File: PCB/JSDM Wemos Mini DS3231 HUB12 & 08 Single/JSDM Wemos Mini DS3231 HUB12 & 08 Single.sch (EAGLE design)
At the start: 14 parts, among them X1 PSU

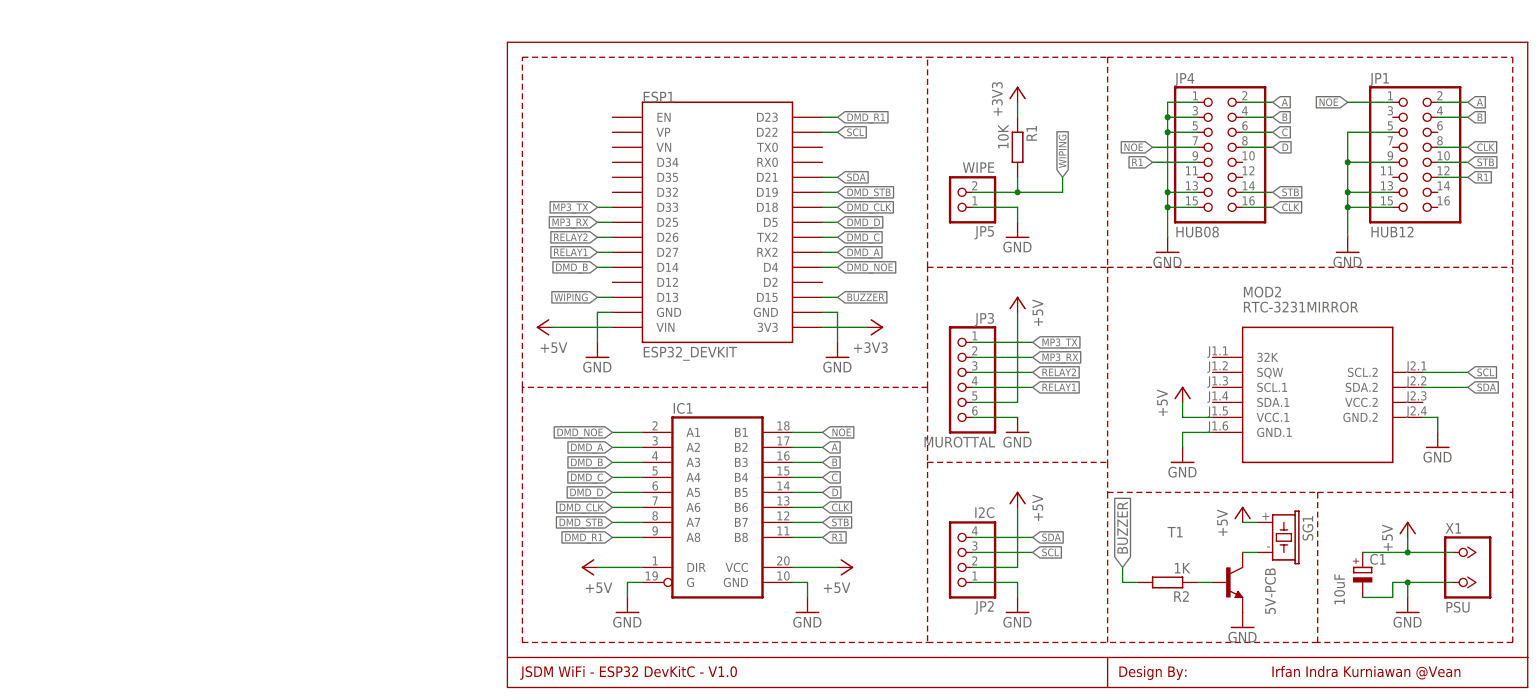
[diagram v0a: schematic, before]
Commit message: JSDM PCB Single Layer ESP8266 + ESP32
Desain PCB SIngle Layer versi:
- Wemos D1 mini HUB12 + HUB08
- Wemos D1 Mini 3x HUB12
- ESP32 Devkit HUB12 + HUB08
- ESP32 Devkit Mini 3x HUB12
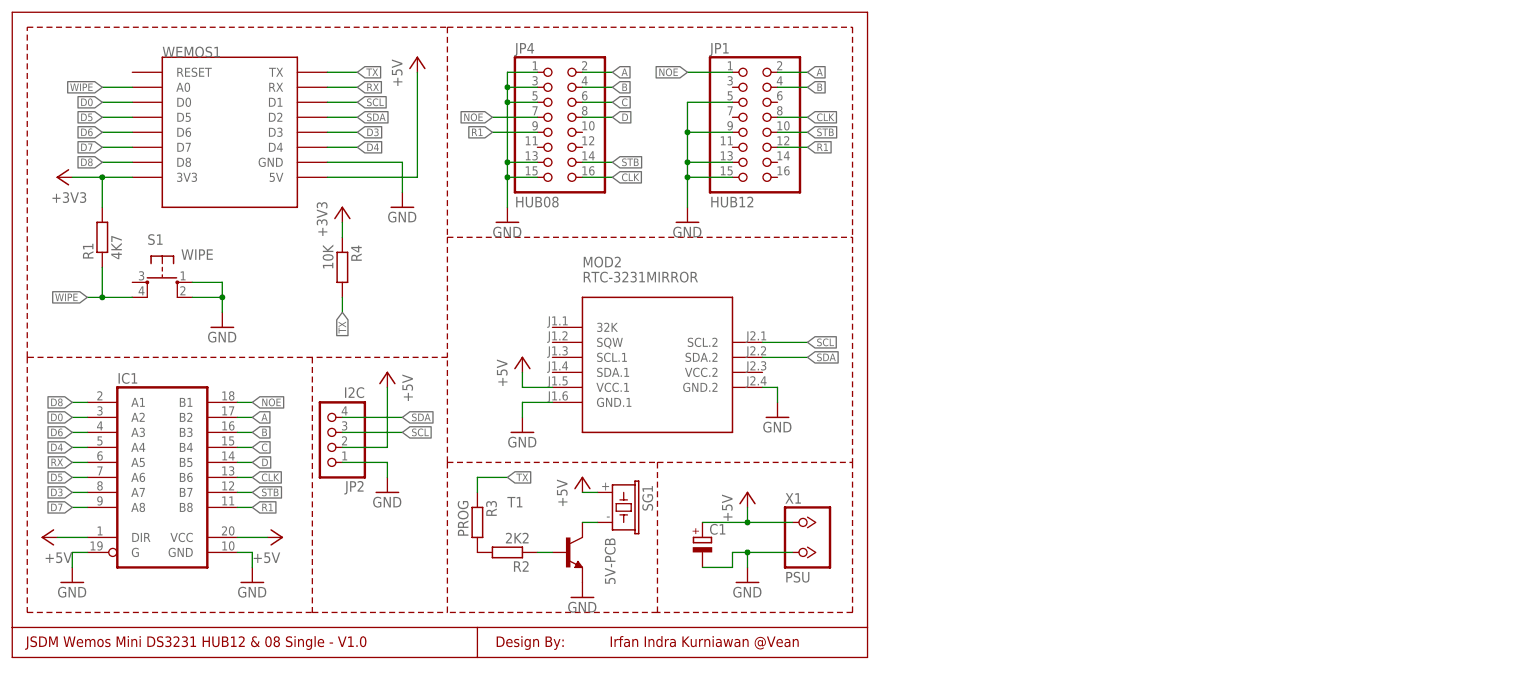
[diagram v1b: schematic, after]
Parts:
- removed ESP1: ESP32_DEVKIT, DOIT_ESP32_DEVKIT:ESP32_DEVKIT
- removed JP3: MUROTTAL, FansElectronics-Header:PINHD-1X6
- removed JP5: WIPE, FansElectronics-Header:PINHD-1X2
- added R3: PROG, FansElectronics-RCL:R-EU_M0805
- added R4: 10K, FansElectronics-RCL:R-EU_0207/12
- added S1: WIPE, FansElectronics-Switch:TACT-6X6OCT
- added WEMOS1: (no value), esp8266modules:WEMOS-D1-MINI
- C1: value 10uF -> (none)
- R1: value 10K -> 4K7; device FansElectronics-RCL:R-EU_0207/7 -> FansElectronics-RCL:R-EU_0207/12
- R2: value 1K -> 2K2; device FansElectronics-RCL:R-EU_0207/10 -> FansElectronics-RCL:R-EU_0207/7
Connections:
- removed net BUZZER: ESP1.D15, R2.2
- removed net DMD_A: ESP1.RX2, IC1.A2
- removed net DMD_B: ESP1.D14, IC1.A3
- removed net DMD_C: ESP1.TX2, IC1.A4
- removed net DMD_CLK: ESP1.D18, IC1.A6
- removed net DMD_D: ESP1.D5, IC1.A5
- removed net DMD_NOE: ESP1.D4, IC1.A1
- removed net DMD_R1: ESP1.D23, IC1.A8
- removed net DMD_STB: ESP1.D19, IC1.A7
- removed net MP3_RX: ESP1.D25, JP3.2
- removed net MP3_TX: ESP1.D33, JP3.1
- removed net RELAY1: ESP1.D27, JP3.4
- removed net RELAY2: ESP1.D26, JP3.3
- removed net WIPING: ESP1.D13, JP5.2, R1.2
- new net D0: IC1.A2, WEMOS1.D0
- new net D3: IC1.A7, WEMOS1.D3
- new net D4: IC1.A4, WEMOS1.D4
- new net D5: IC1.A6, WEMOS1.D5
- new net D6: IC1.A3, WEMOS1.D6
- new net D7: IC1.A8, WEMOS1.D7
- new net D8: IC1.A1, WEMOS1.D8
- new net N$6: R2.2, R3.2
- new net RX: IC1.A5, WEMOS1.RX
- new net TX: R3.1, R4.2, WEMOS1.TX
- new net WIPE: R1.1, S1.P1, WEMOS1.A0
- net +3V3: now also R1.2, R4.1, WEMOS1.3V3; no longer ESP1.3V3, R1.1
- net +5V: now also WEMOS1.5V; no longer ESP1.VIN, JP3.5
- net GND: now also S1.S, S1.S1, WEMOS1.GND; no longer ESP1.GND@1, ESP1.GND@2, JP3.6, JP5.1
- net SCL: now also WEMOS1.D1; no longer ESP1.D22
- net SDA: now also WEMOS1.D2; no longer ESP1.D21
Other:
- note added: "JSDM Wemos Mini DS3231 HUB12 & 08 Single - V1.0"
- note removed: "JSDM WiFi - ESP32 DevKitC - V1.0"
- moved on the sheet: C1, IC1, JP1, JP2, JP4, MOD2, R1, R2, SG1, T1, X1
